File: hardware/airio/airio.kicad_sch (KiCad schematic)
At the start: 25 parts, among them J1 LiPo 1S, J2 GPS, J3 SCREEN, J4 I2C, J5 Buzzer, SW1 TS-1187A-B-A-B, U1 XIAO nRF52840, U2 BMP581, U3 LSM6DSV16X, U4 TCA9534PWR

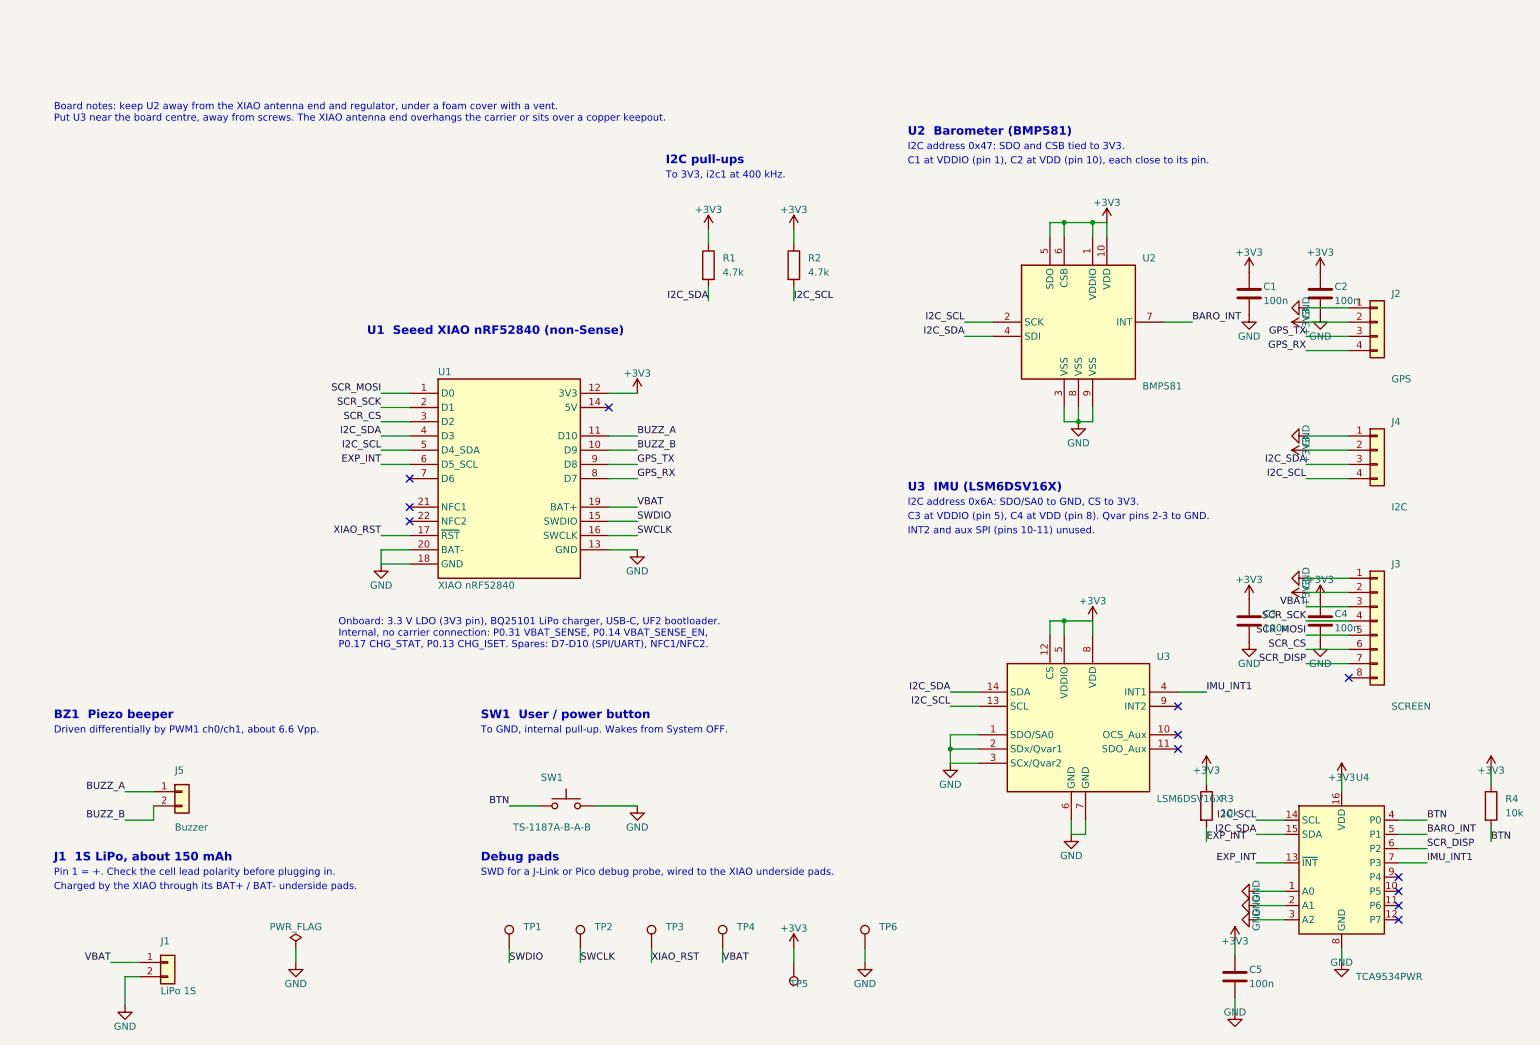
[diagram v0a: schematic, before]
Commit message: airio: J1 to through-hole PH on the back; restore SH ports
- J1 is now JST S2B-PH-K-S (THT, side entry), flipped to the bottom side.
- Max's latest pin assignment: buzzer on D6/D7, GPS on D9/D10 (J2 pin 3
  GPS RX, pin 4 GPS TX), screen on D0-D2 with J3 reordered, BARO_INT on
  U4 P0, IMU_INT1 on P1, SCR_DISP on P2; D8 spare.
- A schematic save from an older editor session had undone the SH change;
  J2/J4 SM04B, J3 SM08B and J5 SM02B (replacing BZ1) are re-applied.
- BTN had lost its expander pin; it is now on U4 P3.
- ERC 0 errors; DRC parity: no footprint mismatches (TP1 missing on the
  board, two duplicate SW1 footprints).

Co-Authored-By: Claude Opus 5.5 (1M context) <noreply@anthropic.com>
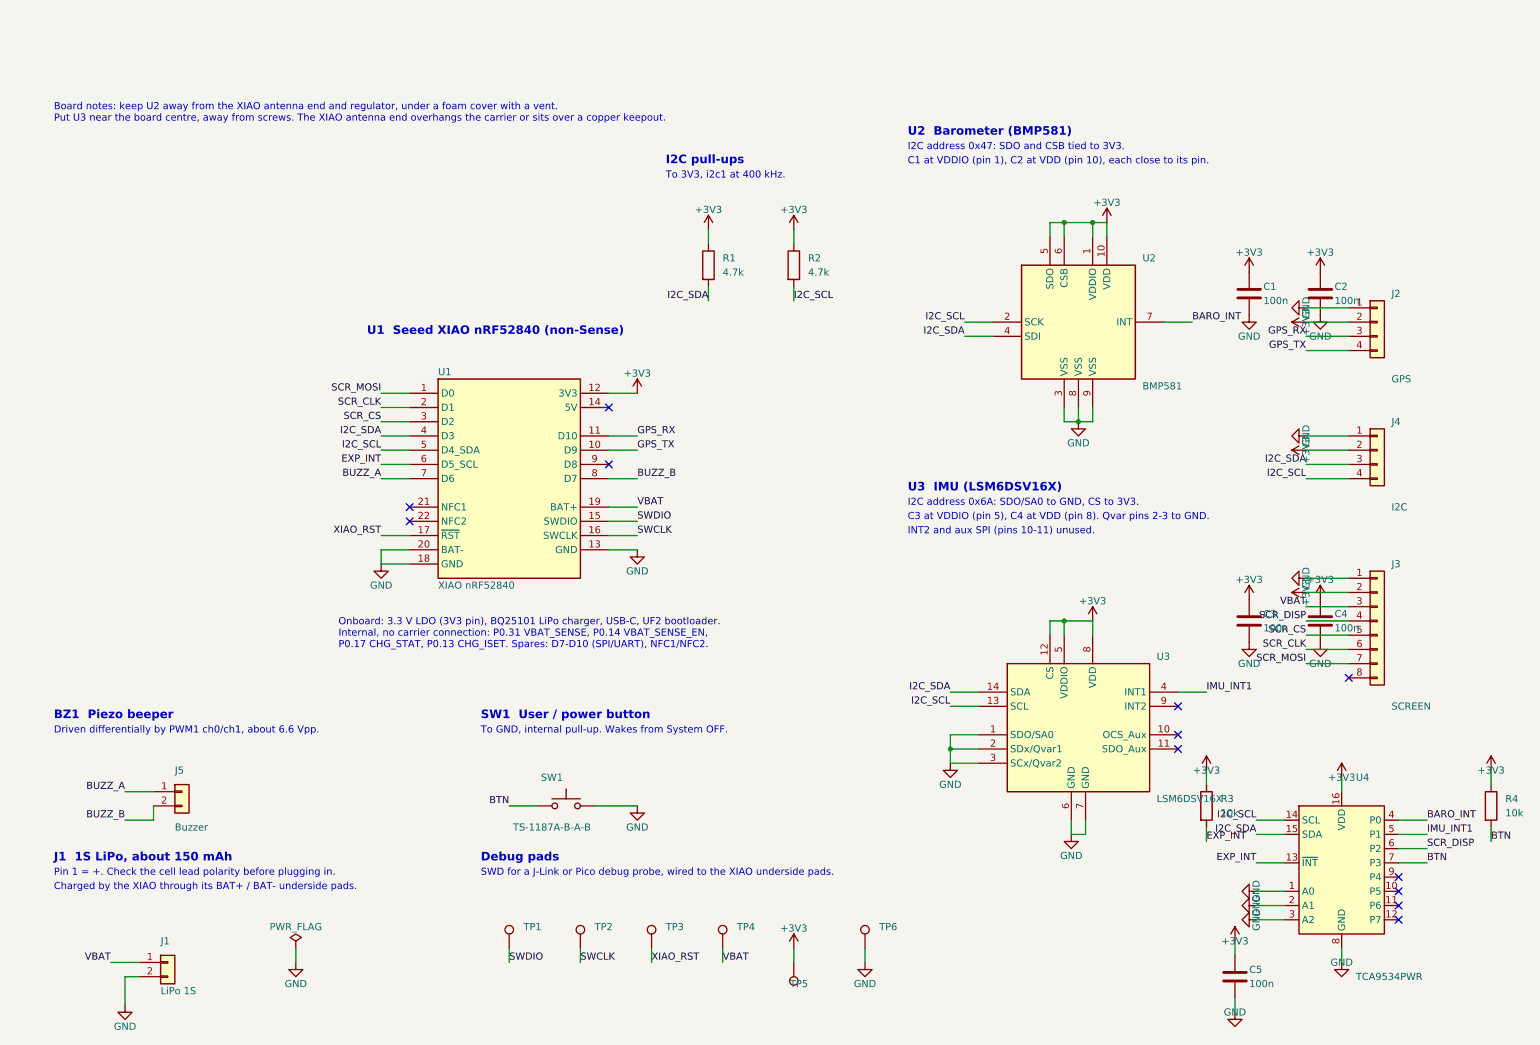
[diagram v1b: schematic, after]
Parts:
- J1: footprint Connector_JST:JST_PH_S2B-PH-SM4-TB_1x02-1MP_P2.00mm_Horizontal -> Connector_JST:JST_PH_S2B-PH-K_1x02_P2.00mm_Horizontal; LCSC C295747 -> C173752; MPN JST S2B-PH-SM4-TB(LF)(SN) -> JST S2B-PH-K-S(LF)(SN)
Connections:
- net BARO_INT: now also U4.4 (P0); no longer U4.5 (P1)
- net BTN: now also U4.7 (P3); no longer U4.4 (P0)
- net BUZZ_A: now also U1.7 (D6); no longer U1.11 (D10)
- net BUZZ_B: now also U1.8 (D7); no longer U1.10 (D9)
- net GPS_RX: now also J2.3 (Pin_3), U1.11 (D10); no longer J2.4 (Pin_4), U1.8 (D7)
- net GPS_TX: now also J2.4 (Pin_4), U1.10 (D9); no longer J2.3 (Pin_3), U1.9 (D8)
- net IMU_INT1: now also U4.5 (P1); no longer U4.7 (P3)
- net SCR_CS: now also J3.5 (Pin_5); no longer J3.6 (Pin_6)
- net SCR_DISP: now also J3.4 (Pin_4); no longer J3.7 (Pin_7)
- net SCR_MOSI: now also J3.7 (Pin_7); no longer J3.5 (Pin_5)
- net SCR_SCK renamed SCR_CLK
- net SCR_CLK: now also J3.6 (Pin_6); no longer J3.4 (Pin_4)
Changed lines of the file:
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@@
 	)
 	(no_connect
-		(at 83.82 93.98)
+		(at 119.38 91.44)
 	)
 	(wire
@@
 	(wire
 		(pts
+			(xy 78.74 93.98) (xy 83.82 93.98)
+		)
+		(stroke
+			(width 0)
+			(type default)
+		)
+	)
+	(wire
+		(pts
 			(xy 218.44 66.04) (xy 223.52 66.04)
 		)
@@
 	(wire
 		(pts
-			(xy 119.38 91.44) (xy 124.46 91.44)
+			(xy 260.35 162.56) (xy 265.43 162.56)
 		)
 		(stroke
@@
 	(wire
 		(pts
+			(xy 38.1 152.4) (xy 38.1 154.94)
+		)
+		(stroke
+			(width 0)
+			(type default)
+		)
+	)
+	(wire
+		(pts
 			(xy 119.38 106.68) (xy 124.46 106.68)
 		)
@@
 	(wire
 		(pts
-			(xy 260.35 162.56) (xy 265.43 162.56)
+			(xy 119.38 86.36) (xy 124.46 86.36)
 		)
 		(stroke
@@
 	(wire
 		(pts
-			(xy 38.1 152.4) (xy 38.1 154.94)
-		)
-		(stroke
-			(width 0)
-			(type default)
-		)
-	)
-	(wire
-		(pts
 			(xy 152.4 52.07) (xy 152.4 49.53)
 		)
@@
 	(wire
 		(pts
-			(xy 119.38 86.36) (xy 124.46 86.36)
-		)
-		(stroke
-			(width 0)
-			(type default)
-		)
-	)
-	(wire
-		(pts
 			(xy 83.82 106.68) (xy 78.74 106.68)
 		)
@@
 		)
 	)
-	(label "BARO_INT"
+	(label "IMU_INT1"
 		(at 265.43 157.48 0)
 		(effects
@@
 		)
 	)
-	(label "IMU_INT1"
-		(at 265.43 162.56 0)
-		(effects
-			(font
-				(size 1.27 1.27)
-			)
-			(justify left bottom)
-		)
-	)
 	(label "I2C_SDA"
 		(at 78.74 86.36 180)
@@
 		)
 	)
-	(label "GPS_TX"
-		(at 124.46 91.44 0)
+	(label "I2C_SCL"
+		(at 234.95 154.94 180)
 		(effects
 			(font
 				(size 1.27 1.27)
 			)
-			(justify left bottom)
+			(justify right bottom)
 		)
 	)
 	(label "BUZZ_A"
-		(at 124.46 86.36 0)
-		(effects
-			(font
-				(size 1.27 1.27)
-			)
-			(justify left bottom)
-		)
-	)
-	(label "I2C_SCL"
-		(at 234.95 154.94 180)
+		(at 78.74 93.98 180)
 		(effects
 			(font
@@
 		)
 	)
-	(label "BUZZ_B"
+	(label "GPS_TX"
 		(at 124.46 88.9 0)
 		(effects
@@
 		)
 	)
-	(label "SCR_MOSI"
+	(label "SCR_CS"
 		(at 243.84 121.92 180)
 		(effects
@@
 		)
 	)
-	(label "SCR_DISP"
+	(label "SCR_MOSI"
 		(at 243.84 127 180)
 		(effects
@@
 		)
 	)
-	(label "SCR_SCK"
+	(label "SCR_DISP"
 		(at 243.84 119.38 180)
 		(effects
@@
 		)
 	)
-	(label "SCR_SCK"
+	(label "SCR_CLK"
 		(at 78.74 81.28 180)
 		(effects
@@
 		)
 	)
+	(label "GPS_RX"
+		(at 124.46 86.36 0)
+		(effects
+			(font
+				(size 1.27 1.27)
+			)
+			(justify left bottom)
+		)
+	)
 	(label "SCR_DISP"
 		(at 265.43 160.02 0)
@@
 		)
 	)
-	(label "BTN"
+	(label "BARO_INT"
 		(at 265.43 154.94 0)
 		(effects
@@
 		)
 	)
-	(label "SCR_CS"
+	(label "SCR_CLK"
 		(at 243.84 124.46 180)
 		(effects
@@
 		)
 	)
-	(label "GPS_TX"
+	(label "BTN"
+		(at 265.43 162.56 0)
+		(effects
+			(font
+				(size 1.27 1.27)
+			)
+			(justify left bottom)
+		)
+	)
+	(label "GPS_RX"
 		(at 243.84 68.58 180)
 		(effects
@@
 		)
 	)
-	(label "GPS_RX"
+	(label "GPS_TX"
 		(at 243.84 71.12 180)
 		(effects
@@
 		)
 	)
-	(label "GPS_RX"
+	(label "BUZZ_B"
 		(at 124.46 93.98 0)
 		(effects
@@
 			)
 		)
-		(property "Footprint" "Connector_JST:JST_PH_S2B-PH-SM4-TB_1x02-1MP_P2.00mm_Horizontal"
+		(property "Footprint" "Connector_JST:JST_PH_S2B-PH-K_1x02_P2.00mm_Horizontal"
 			(at 40.64 180.34 0)
 			(hide yes)
@@
 			)
 		)
-		(property "LCSC" "C295747"
+		(property "LCSC" "C173752"
 			(at 40.64 180.34 0)
 			(hide yes)
@@
 			)
 		)
-		(property "MPN" "JST S2B-PH-SM4-TB(LF)(SN)"
+		(property "MPN" "JST S2B-PH-K-S(LF)(SN)"
 			(at 40.64 180.34 0)
 			(hide yes)

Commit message: airio: add J6 FPC for bare ST7305 2.9in panel, C6-C12, D8 as SCR_DC
J6 is an HCTL HC-FPC-05-09-24RLTAG (C5213757) 24-pin 0.5 mm FPC for an
Osptek YDP290H001-V3 / Good Display GDTL029T51 reflective panel. Panel
rails VGH, VGL, AVDD, VIV and VNV get 1 uF each (C6-C10) and VCI/IOVCC get
1 uF each (C11-C12), all CL10A105KB8NNNC (C15849). RES shares SCR_DISP,
D/C is a new SCR_DC net on D8, also routed to J3 pin 8.

Co-Authored-By: Claude Opus 5.5 (1M context) <noreply@anthropic.com>
Claude-Session: https://claude.ai/code/session_013dGQQirkDZBqDrtnyirHTc
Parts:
- added C10, C11, C12, C6, C7, C8, C9: 1u, Capacitor_SMD:C_0603_1608Metric, symbol Device:C
- added J6: ST7305 FPC, Connector_FFC-FPC:Hirose_FH12-24S-0.5SH_1x24-1MP_P0.50mm_Horizontal, symbol Connector_Generic:Conn_01x24
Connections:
- net +3V3: now also C11.1, C12.1, J6.15 (Pin_15), J6.16 (Pin_16), J6.5 (Pin_5)
- net GND: now also C10.2, C11.2, C12.2, C6.2, C7.2, C8.2, C9.2, J6.17 (Pin_17)
- net SCR_CLK: now also J6.13 (Pin_13)
- net SCR_CS: now also J6.12 (Pin_12)
- net SCR_DISP: now also J6.10 (Pin_10)
- net SCR_MOSI: now also J6.14 (Pin_14)
- net SCR_DC: now reaches U1.9 (D8)
- net SCR_DC: now also J3.8 (Pin_8), J6.11 (Pin_11)
- new net SCR_AVDD: C8.1, J6.21 (Pin_21)
- new net SCR_VGH: C6.1, J6.18 (Pin_18)
- new net SCR_VGL: C7.1, J6.24 (Pin_24)
- new net SCR_VIV: C9.1, J6.20 (Pin_20)
- new net SCR_VNV: C10.1, J6.22 (Pin_22)
- no-connect marks 12 -> 20
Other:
- note added: "C6-C12 1 uF 0603 X5R 50 V, at J6: VGH, VGL, AVDD, VIV, VNV outputs; C11 VCI (16), C12 IOVCC (15)."
- note added: "Footprint is a placeholder (Hirose FH12): check pads against the HCTL drawing."
- note added: "J6 2.9in ST7305 reflective panel, 24-pin 0.5 mm FPC (Osptek YDP290H001-V3 / Good Display GDTL029T51)"
- note added: "RES on SCR_DISP (U4 P2). D/C on D8. CS active low. TE (9) unused."
